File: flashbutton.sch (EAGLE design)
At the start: 3 parts

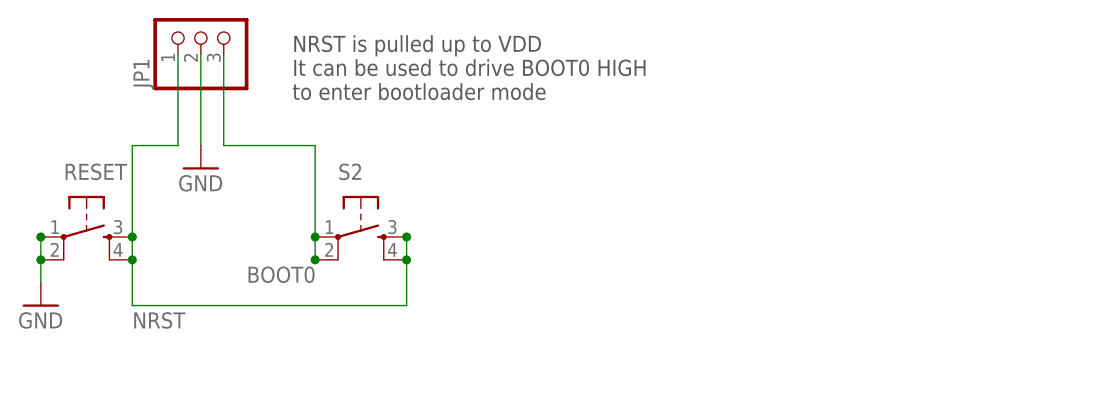
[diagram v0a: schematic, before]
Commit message: added a note about how to patch the board for this
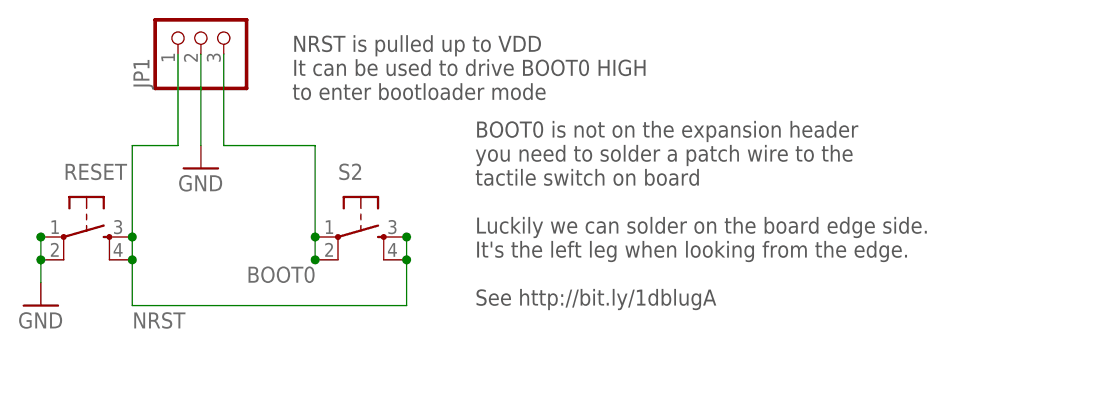
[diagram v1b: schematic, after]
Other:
- note added: "BOOT0 is not on the expansion header you need to solder a patch wire to the tactile switch on board Luckily we can solder on the board edge side. It's the left leg when looking from the edge. See http://bit.ly/1dblugA"
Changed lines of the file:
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@@
 It can be used to drive BOOT0 HIGH
 to enter bootloader mode</text>
+<text x="78.74" y="40.64" size="1.778" layer="97">BOOT0 is not on the expansion header
+you need to solder a patch wire to the
+tactile switch on board
+Luckily we can solder on the board edge side.
+It's the left leg when looking from the edge.
+See http://bit.ly/1dblugA</text>
 </plain>
 <instances>

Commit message: notes on c2
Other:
- note added: "RevC1: BOOT0 is not on the expansion header you need to solder a patch wire to the tactile switch on board Luckily we can solder on the board edge side. It's the left leg when looking from the edge. See http://bit.ly/1dblugA RevC2: See http://bit.ly/OtoQXh for pinout."
- note removed: "BOOT0 is not on the expansion header you need to solder a patch wire to the tactile switch on board Luckily we can solder on the board edge side. It's the left leg when looking from the edge. See http://bit.ly/1dblugA"
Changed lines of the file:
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@@
 It can be used to drive BOOT0 HIGH
 to enter bootloader mode</text>
-<text x="78.74" y="40.64" size="1.778" layer="97">BOOT0 is not on the expansion header
+<text x="78.74" y="33.02" size="1.778" layer="97">RevC1: BOOT0 is not on the expansion header
 you need to solder a patch wire to the
 tactile switch on board
 Luckily we can solder on the board edge side.
 It's the left leg when looking from the edge.
-See http://bit.ly/1dblugA</text>
+See http://bit.ly/1dblugA
+RevC2: See http://bit.ly/OtoQXh for pinout.</text>
 </plain>
 <instances>
